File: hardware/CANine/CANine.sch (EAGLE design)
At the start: 23 parts, among them J1 UJ2-MIBH2-4-SMT-TR, J5 DF13A-4P-1.25H(21), U1 STM32F042C6T6, U2 AP2202K-3.3TRG1, U3 MCP2551

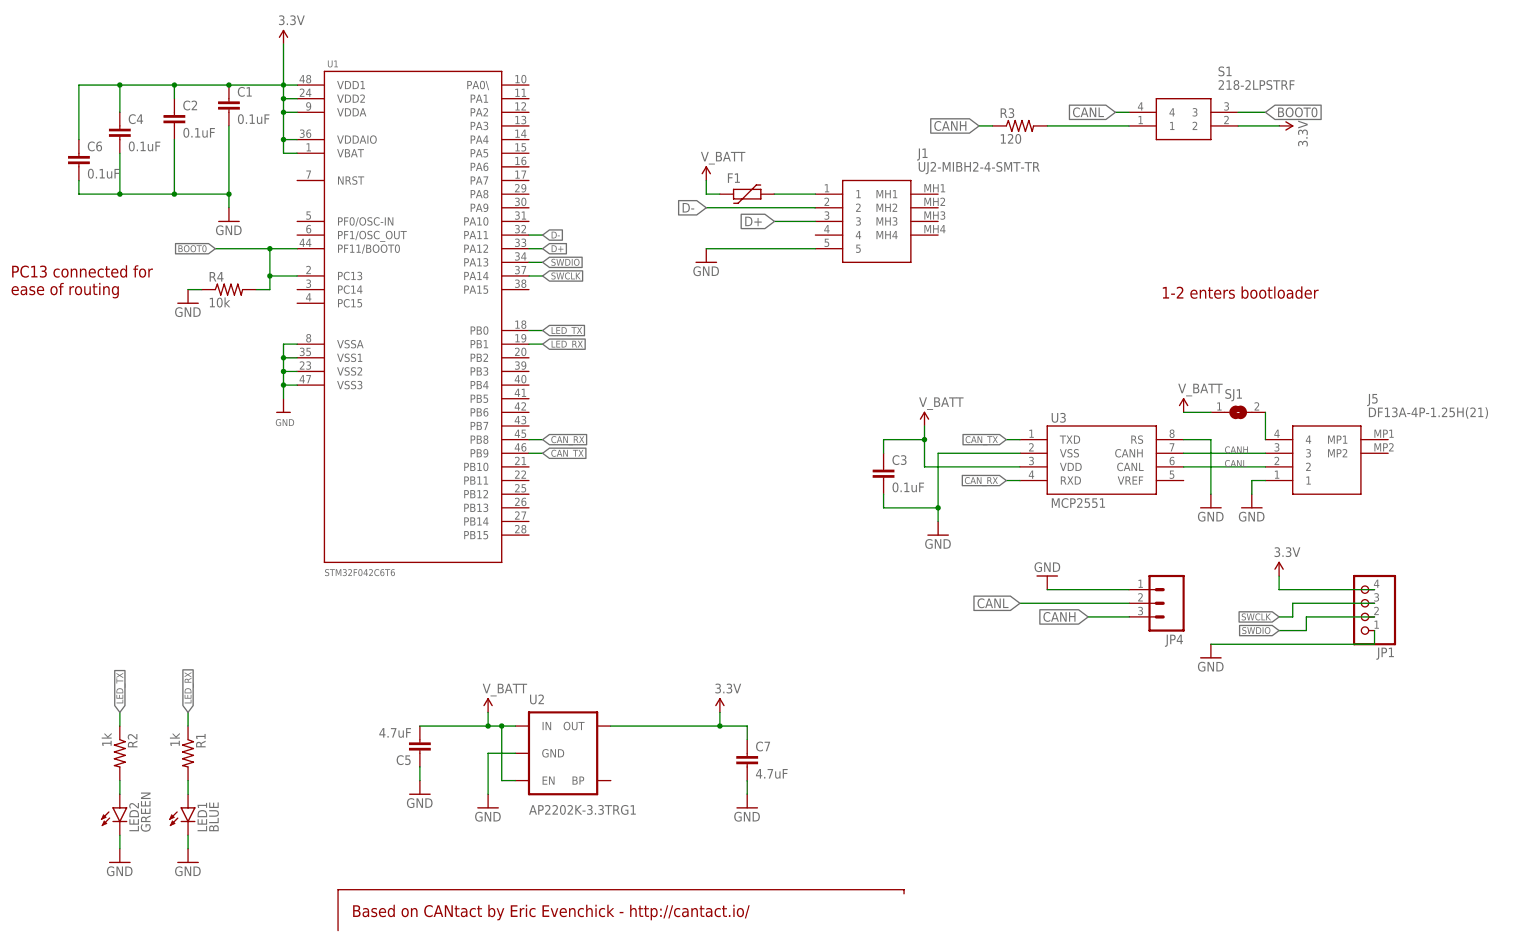
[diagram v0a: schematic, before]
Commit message: Update CANine CAN Adapter schematics and models (#77)
* update can adapter

* update case
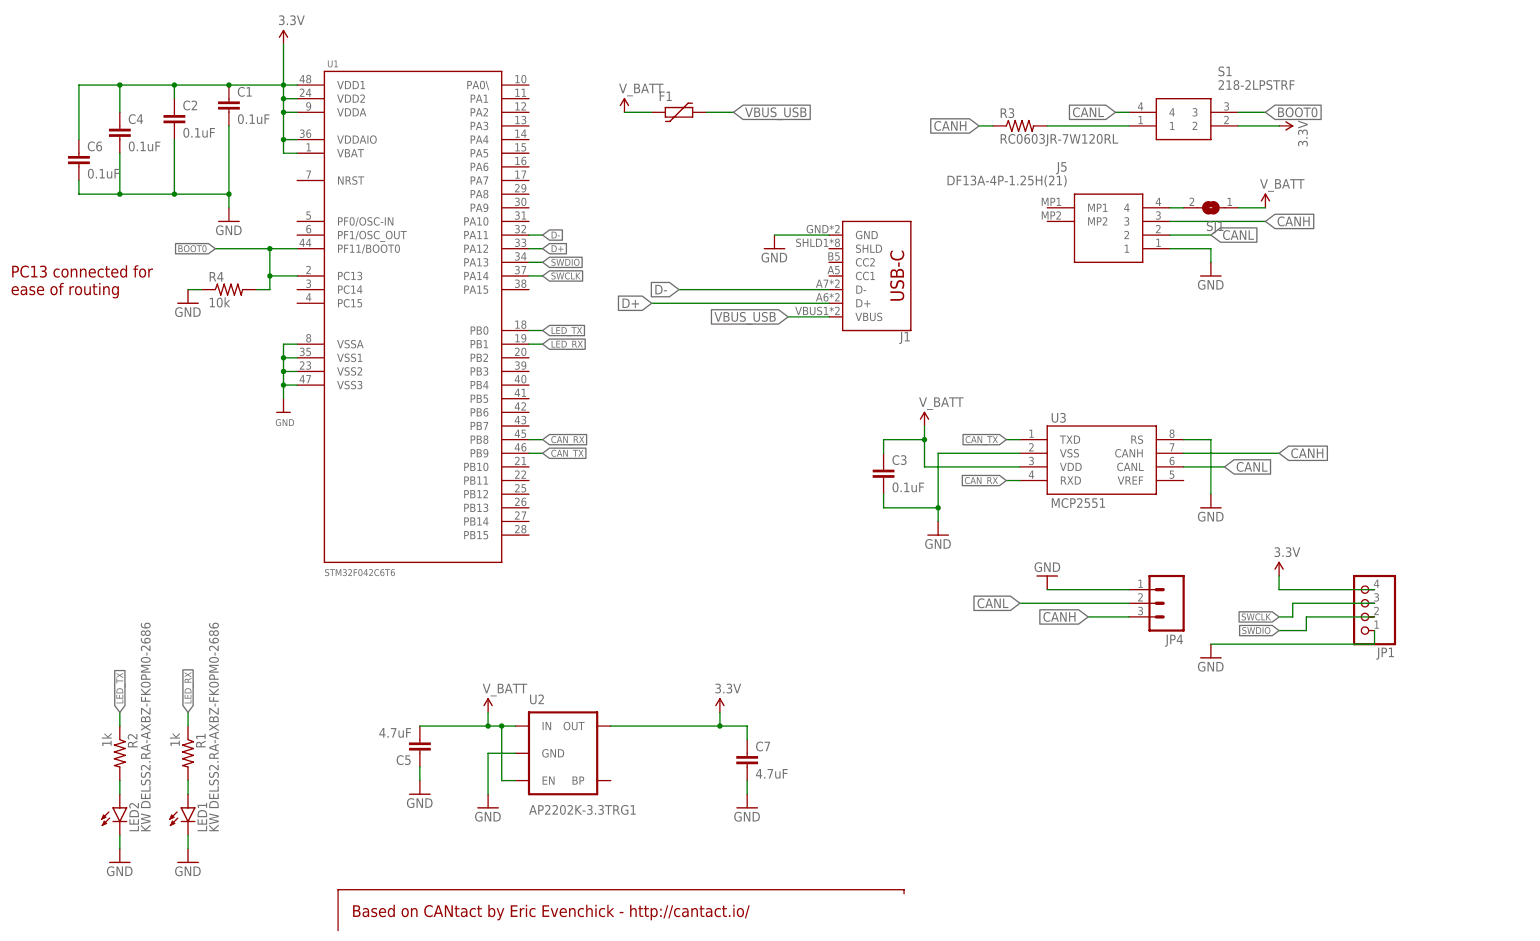
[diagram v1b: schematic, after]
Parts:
- J1: value UJ2-MIBH2-4-SMT-TR -> (none); device SamacSys_Parts:UJ2-MIBH2-4-SMT-TR -> USB-C-Breakout:SPARKFUN-CONNECTORS_USB_C16PIN
- LED1: value BLUE -> KW DELSS2.RA-AXBZ-FK0PM0-2686
- LED2: value GREEN -> KW DELSS2.RA-AXBZ-FK0PM0-2686
- R3: value 120 -> RC0603JR-7W120RL
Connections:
- removed net N$7: F1.2, J1.1
- new net VBUS_USB: F1.2, J1.VBUS
- net D+: now also J1.D+; no longer J1.3
- net D-: now also J1.D-; no longer J1.2
- net GND: now also J1.GND; no longer J1.5
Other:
- note removed: "1-2 enters bootloader"
- moved on the sheet: F1, J5, SJ1
